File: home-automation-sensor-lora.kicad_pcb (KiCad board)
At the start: 4 copper layers, 96.5 x 96.5 mm, 121 parts, among them J1 Thermistor, J2 Conn_01x08, J3 Stemma-QT-Connector, J4 USB4105-GF-A_Lizard, J5 3V3-16V, J6 Conn_01x04, Q1 DMN2046U-7, Q2 DMN2046U-7, Q3 DMG3415U-13, U1 LD2985BM33R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

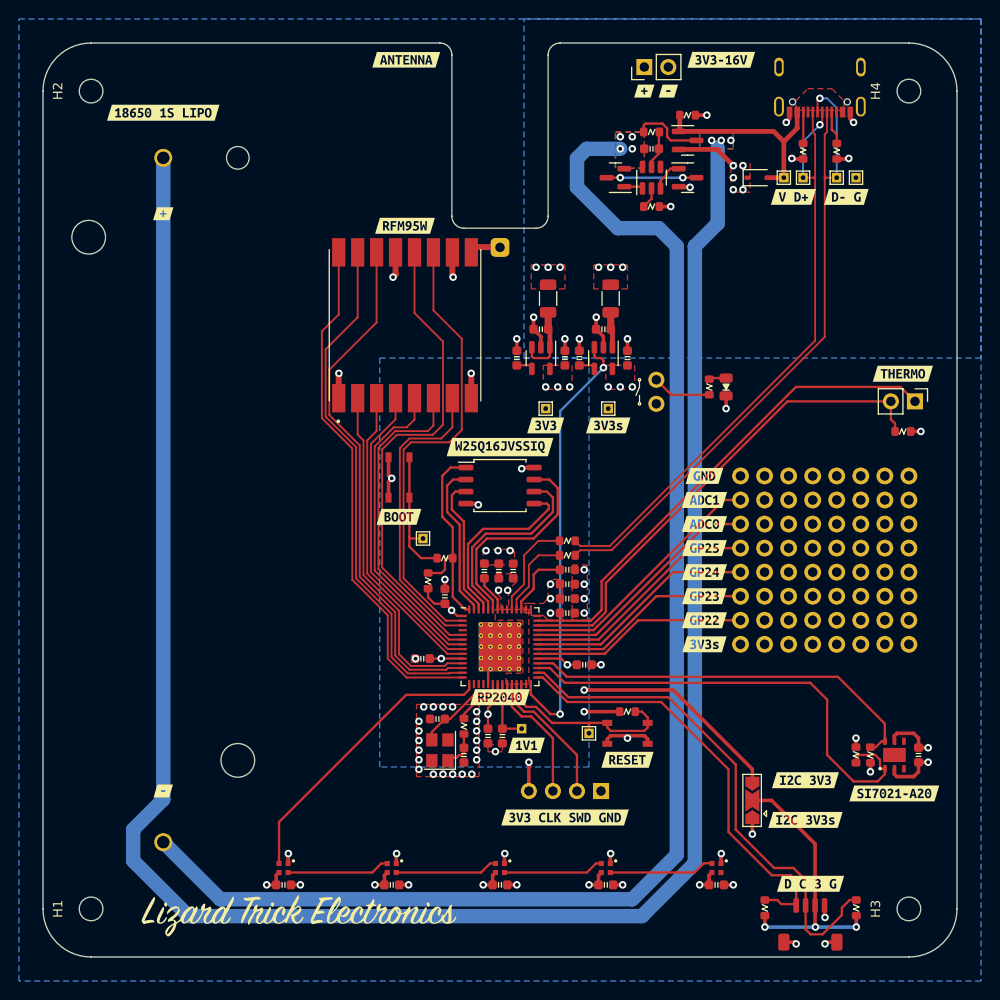
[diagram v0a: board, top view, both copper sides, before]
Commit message: Updated RP2040 footprint and updated routing to accommodate it
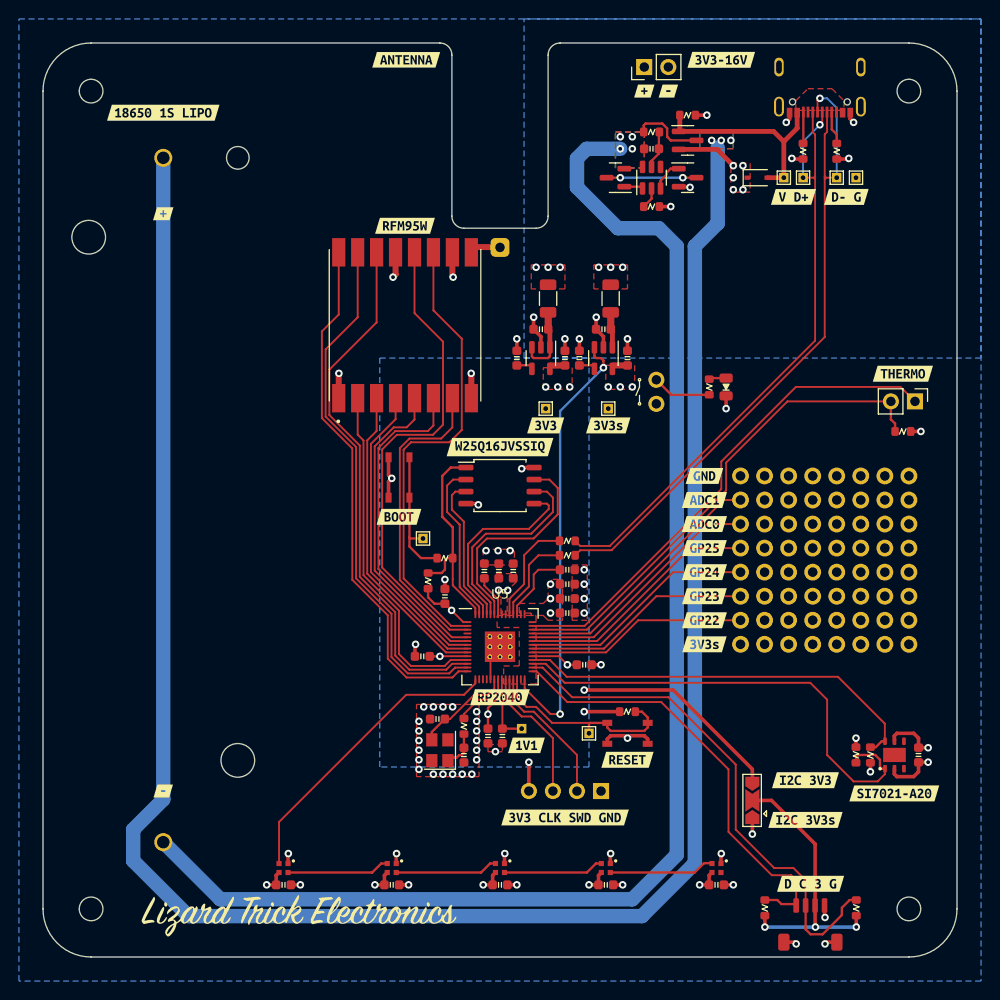
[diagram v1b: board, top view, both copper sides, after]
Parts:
- BT1: value 18650 -> Keystone 1043 18650
- C3, C6: value 30p -> 15p
- U5: footprint Package_DFN_QFN:QFN-56-1EP_8x8mm_P0.5mm_EP4.5x5.2mm_ThermalVias -> lizard_libs:RP2040_QFN-56
- moved C12 0.24 mm to (162.5, 96.0)
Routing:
- net +3V3: track 49.4 -> 53.3 mm
- net GND: track 65.6 -> 67.8 mm
- net +1V1: track 18.0 -> 19.7 mm
- net +3V3_S: track 23.3 -> 24.8 mm
- net 3V3_S_EN: track 46.4 -> 47.1 mm
- net SDA1: track 46.1 -> 46.8 mm
- net LORA_DIO2: track 55.3 -> 56.0 mm
- net NEOPIXEL: track 30.8 -> 31.6 mm
- net LORA_DIO3: track 48.7 -> 49.4 mm
- net SCL1: track 54.1 -> 54.9 mm
- net LORA_DIO1: track 55.3 -> 56.0 mm
- net /QSPI_SD1: track 16.5 -> 17.2 mm
- net Net-(U5-RUN): track 20.7 -> 21.4 mm
- net LORA_DIO5: track 32.1 -> 32.8 mm
- net SDA: track 50.8 -> 51.5 mm
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
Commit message: Added test points to BMS chip.
Tested BMS functionality and it is not working. It will prevent the battery from being charged at a high voltage, but it will not allow the battery to discharge under normal conditions. Interestingly, attaching 5V to VBUS or VCC while the battery is installed, then removing it, will "kick start" the BMS and allow discharging from the battery.
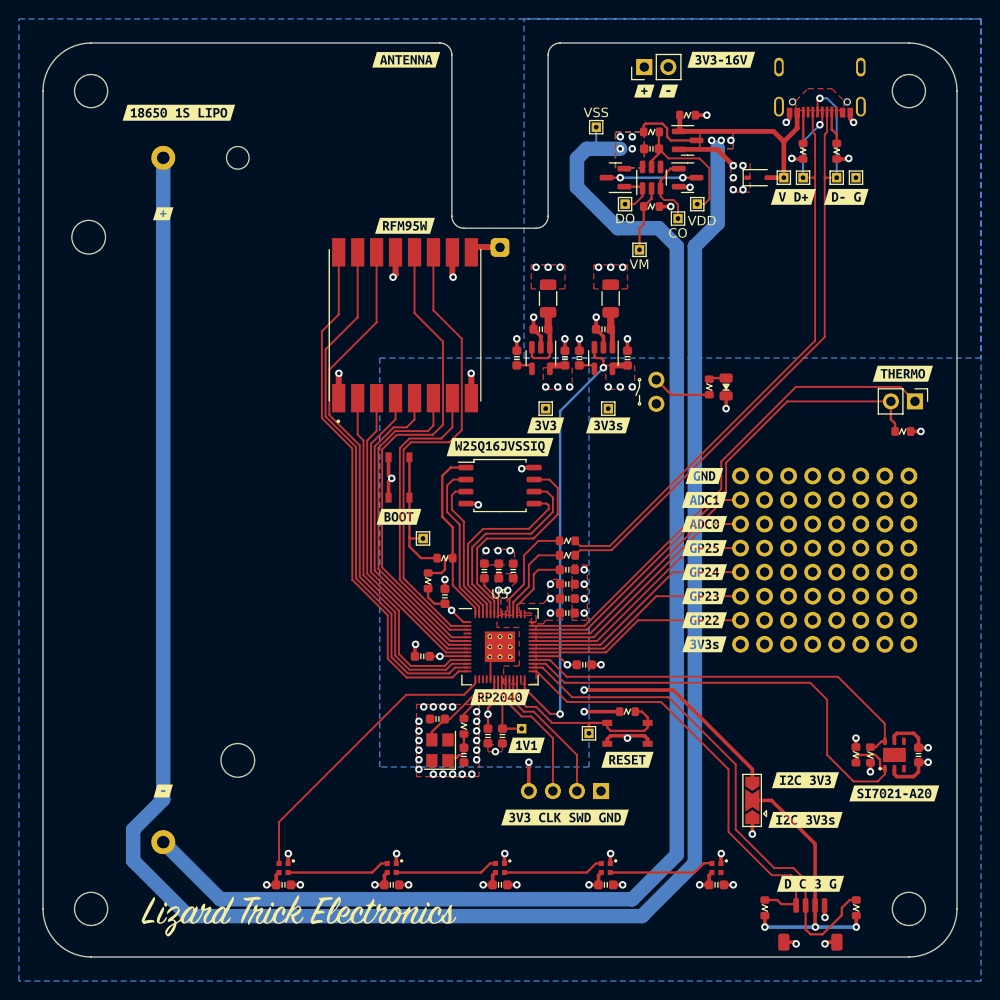
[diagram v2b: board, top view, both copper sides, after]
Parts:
- added TP10: VM, lizard_libs:TestPoint_THTPad_1.0x1.0mm_Drill0.5mm-Lizard, F.Cu at (185.5, 53.1)
- added TP11: VSS, lizard_libs:TestPoint_THTPad_1.0x1.0mm_Drill0.5mm-Lizard, F.Cu at (180.9, 40.2)
- added TP12: VDD, lizard_libs:TestPoint_THTPad_1.0x1.0mm_Drill0.5mm-Lizard, F.Cu at (191.6, 48.3)
- added TP13: CO, lizard_libs:TestPoint_THTPad_1.0x1.0mm_Drill0.5mm-Lizard, F.Cu at (189.5, 49.8)
- added TP14: DO, lizard_libs:TestPoint_THTPad_1.0x1.0mm_Drill0.5mm-Lizard, F.Cu at (183.9, 48.3)
- H1, H2, H3, H4: footprint lizard_libs:MountingHole_2.5mm_Mask -> lizard_libs:Lizard_MountingHole_3.5mm
- moved kibuzzard-63B32B21 1.65 mm to (136.8, 38.6)
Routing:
- net Net-(U7-VDD): track 4.03 -> 15.0 mm
- net Net-(U7-VM): track 2.25 -> 7.01 mm
- net Net-(Q2-G): track 3.39 -> 7.91 mm
- net Net-(Q1-G): track 2.00 -> 5.02 mm
- net /BATT_MINUS: track 144.3 -> 146.6 mm

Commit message: Adjusted power planes around BMS
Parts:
- Q3: value DMG3415U-13 -> DMG3415U-7
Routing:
- net /BATT_MINUS: vias 4 -> 3
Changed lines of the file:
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@@
     (property "ki_description" "test point")
     (property "ki_keywords" "test point tp")
-    (attr exclude_from_pos_files exclude_from_bom)
+    (attr exclude_from_pos_files)
     (fp_text reference "TP12" (at 0 -1.448) (layer "F.Fab")
         (effects (font (size 1 1) (thickness 0.15)))
@@
     (property "ki_description" "test point")
     (property "ki_keywords" "test point tp")
-    (attr exclude_from_pos_files exclude_from_bom)
+    (attr exclude_from_pos_files)
     (fp_text reference "TP14" (at 0 -1.448) (layer "F.Fab")
         (effects (font (size 1 1) (thickness 0.15)))
@@
     (property "ki_description" "test point")
     (property "ki_keywords" "test point tp")
-    (attr exclude_from_pos_files exclude_from_bom)
+    (attr exclude_from_pos_files)
     (fp_text reference "TP13" (at 0 -1.448) (layer "F.Fab")
         (effects (font (size 1 1) (thickness 0.15)))
@@
     (property "ki_description" "test point")
     (property "ki_keywords" "test point tp")
-    (attr exclude_from_pos_files exclude_from_bom)
+    (attr exclude_from_pos_files)
     (fp_text reference "TP10" (at 0 -1.448) (layer "F.Fab")
         (effects (font (size 1 1) (thickness 0.15)))
@@
         (effects (font (size 1 1) (thickness 0.15)))
     )
-    (fp_text value "DMG3415U-13" (at 0 2.4) (layer "F.Fab")
+    (fp_text value "DMG3415U-7" (at 0 2.4) (layer "F.Fab")
         (effects (font (size 1 1) (thickness 0.15)))
     )
@@
     (property "ki_description" "test point")
     (property "ki_keywords" "test point tp")
-    (attr exclude_from_pos_files exclude_from_bom)
+    (attr exclude_from_pos_files)
     (fp_text reference "TP11" (at 0 -1.448) (layer "F.Fab")
         (effects (font (size 1 1) (thickness 0.15)))
@@
   (segment (start 183.937001 48.293001) (end 184.953001 48.293001) (width 0.2032) (layer "F.Cu") (net 64))
   (segment (start 185.781001 42.626001) (end 185.956001 42.451001) (width 0.25) (layer "F.Cu") (net 65))
-  (via (at 183.429001 41.181001) (size 0.8) (drill 0.4) (layers "F.Cu" "B.Cu") (free) (net 65))
-  (via (at 184.699001 41.181001) (size 0.8) (drill 0.4) (layers "F.Cu" "B.Cu") (free) (net 65))
   (via (at 184.699001 42.451001) (size 0.8) (drill 0.4) (layers "F.Cu" "B.Cu") (free) (net 65))
   (via (at 183.429001 42.451001) (size 0.8) (drill 0.4) (layers "F.Cu" "B.Cu") (free) (net 65))
+  (via (at 182.159001 42.451001) (size 0.8) (drill 0.4) (layers "F.Cu" "B.Cu") (free) (net 65))
   (segment (start 135.169001 115.666501) (end 141.201501 121.699001) (width 1.524) (layer "B.Cu") (net 65))
   (segment (start 184.699001 121.699001) (end 189.398001 117.000001) (width 1.524) (layer "B.Cu") (net 65))
@@
       (pts
         (xy 185.969001 44.483001)
-        (xy 182.921001 44.483001)
-        (xy 182.921001 40.673001)
-        (xy 185.969001 40.673001)
+        (xy 182.667001 44.483001)
+        (xy 181.651001 43.467001)
+        (xy 181.651001 41.689001)
+        (xy 185.969001 41.689001)
       )
     )
